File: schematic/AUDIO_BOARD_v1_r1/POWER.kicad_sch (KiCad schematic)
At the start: 10 parts, among them U20 DAC8565, U21 MCP23S17, U22 AP2112K-3.3

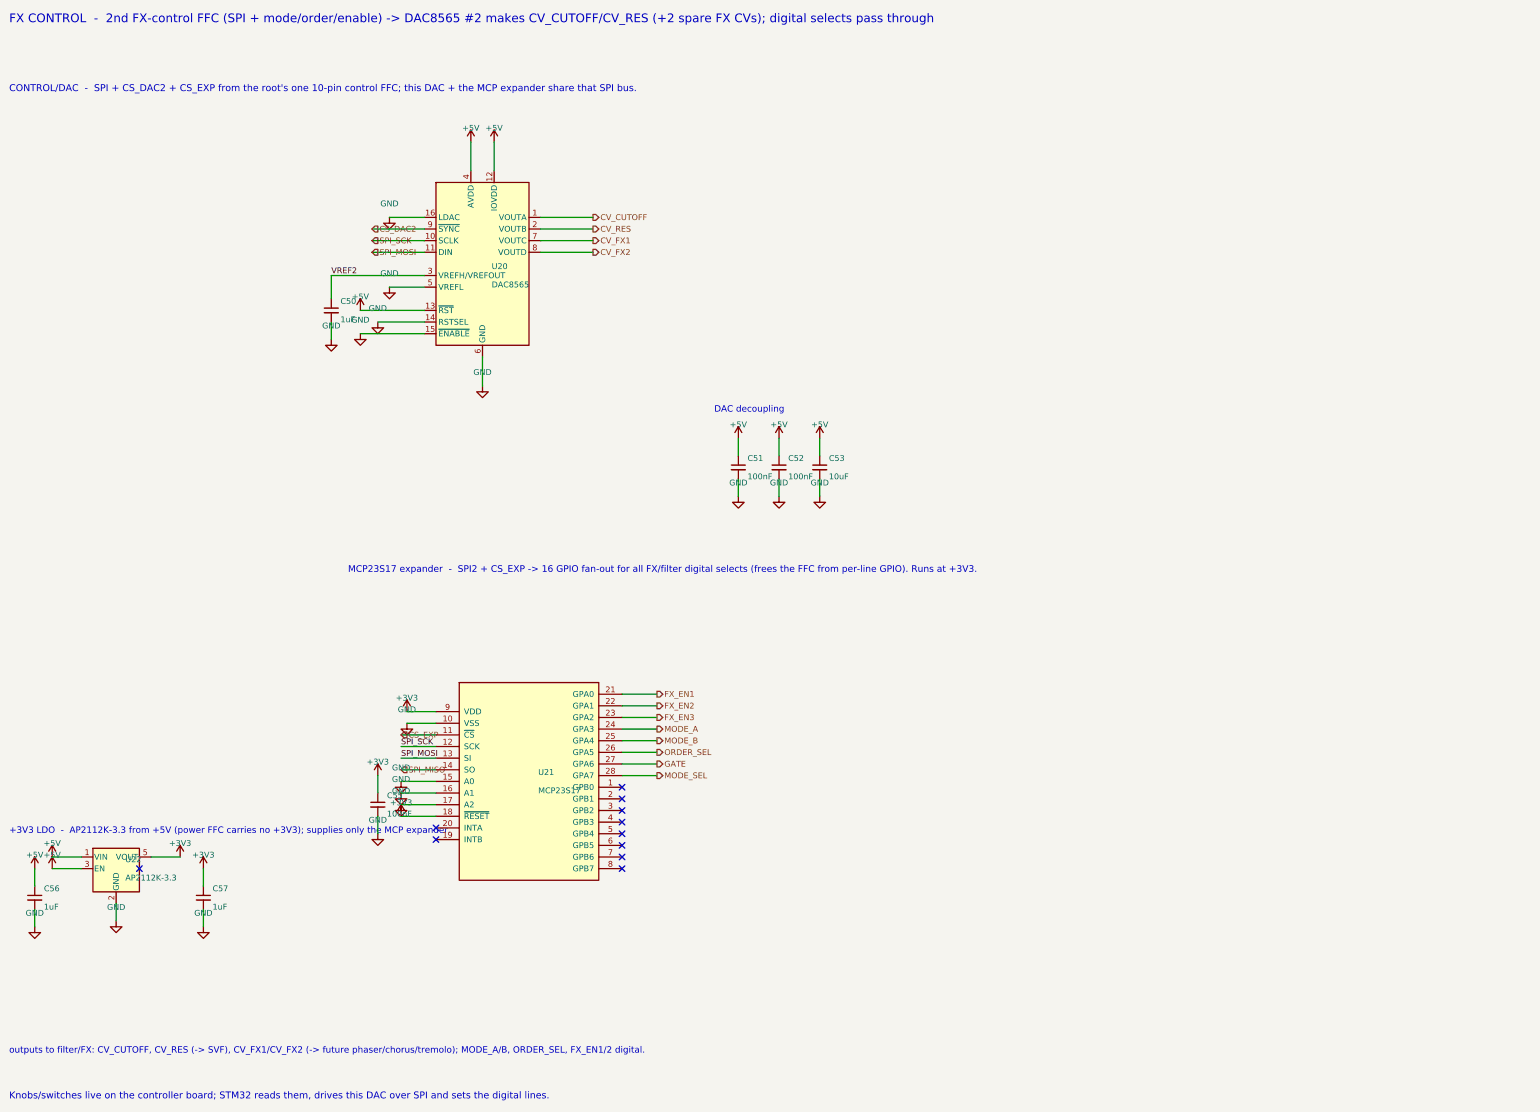
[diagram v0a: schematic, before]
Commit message: placing buffer for output. soft amp going, maybe AB rated. more routing
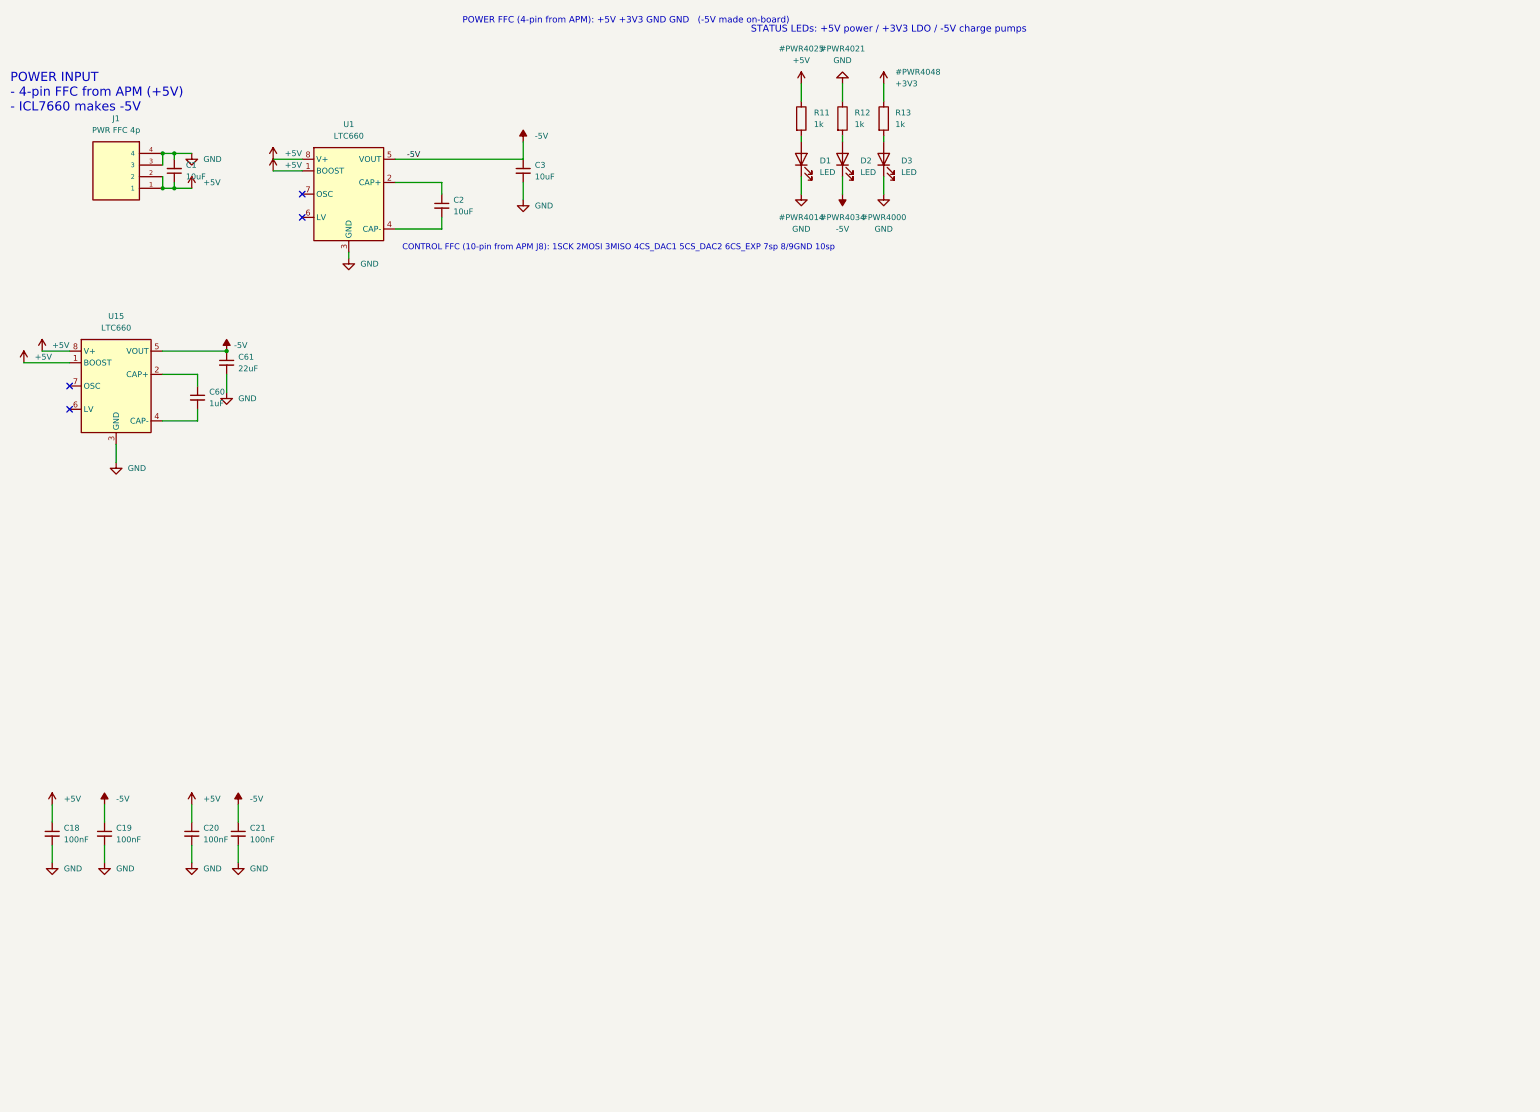
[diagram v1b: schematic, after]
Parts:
- removed C50, C56, C57: 1uF, Capacitor_SMD:C_0402_1005Metric, symbol Device:C_Small
- removed C51, C52, C55: 100nF, Capacitor_SMD:C_0402_1005Metric, symbol Device:C_Small
- removed C53: 10uF, Capacitor_SMD:C_0805_2012Metric, symbol Device:C_Small
- removed U20: DAC8565, Package_SO:TSSOP-16_4.4x5mm_P0.65mm, symbol Analog_DAC:DAC8565
- removed U21: MCP23S17, Package_SO:SOIC-28W_7.5x17.9mm_P1.27mm, symbol Custom:MCP23S17
- removed U22: AP2112K-3.3, Package_TO_SOT_SMD:SOT-23-5, symbol Regulator_Linear:AP2112K-3.3
- added C1, C2, C3: 10uF, Capacitor_SMD:C_0805_2012Metric, symbol Device:C_Small
- added C18, C19, C20, C21: 100nF, Capacitor_SMD:C_0402_1005Metric, symbol Device:C_Small
- added C60: 1uF, Capacitor_SMD:C_0805_2012Metric, symbol Device:C_Small
- added C61: 22uF, Capacitor_SMD:C_0805_2012Metric, symbol Device:C_Small
- added D1, D2, D3: LED, LED_SMD:LED_0603_1608Metric, symbol Device:LED
- added J1: PWR FFC 4p, my_footprints:AMPHENOL_F3311A7H121004E200, symbol F3311A7H121004E200:F3311A7H121004E200
- added R11, R12, R13: 1k, Resistor_SMD:R_0402_1005Metric, symbol Device:R
- added U1, U15: LTC660, Package_SO:SOIC-8_3.9x4.9mm_P1.27mm, symbol Regulator_SwitchedCapacitor:LTC660
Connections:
- net +3V3: now also R13.1
- net +5V: now also C1.1, C18.1, C20.1, J1.1, J1.2, R11.1, U1.1 (BOOST), U1.8 (V+), U15.1 (BOOST), U15.8 (V+)
- net GND: now also C1.2, C18.2, C19.2, C20.2, C21.2, C3.2, C61.2, D1.1 (K), D3.1 (K), J1.3, J1.4, R12.1, U1.3 (GND), U15.3 (GND)
- new net: C2.1, U1.2 (CAP+)
- new net: C2.2, U1.4 (CAP-)
- new net: D1.2 (A), R11.2
- new net: C60.1, U15.2 (CAP+)
- new net: C60.2, U15.4 (CAP-)
- new net: D2.2 (A), R12.2
- new net: D3.2 (A), R13.2
- new net -5V: C19.1, C21.1, C3.1, C61.1, D2.1 (K), U1.5 (VOUT), U15.5 (VOUT)
- no-connect marks 11 -> 4
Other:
- note added: "CONTROL FFC (10-pin from APM J8): 1SCK 2MOSI 3MISO 4CS_DAC1 5CS_DAC2 6CS_EXP 7sp 8/9GND 10sp"
- note added: "POWER FFC (4-pin from APM): +5V +3V3 GND GND (-5V made on-board)"
- note added: "POWER INPUT - 4-pin FFC from APM (+5V) - ICL7660 makes -5V"
- note added: "STATUS LEDs: +5V power / +3V3 LDO / -5V charge pumps"
- note removed: "+3V3 LDO - AP2112K-3.3 from +5V (power FFC carries no +3V3); supplies only the MCP expander."
- note removed: "CONTROL/DAC - SPI + CS_DAC2 + CS_EXP from the root's one 10-pin control FFC; this DAC + the MCP expander share that SPI bus."
- note removed: "DAC decoupling"
- note removed: "FX CONTROL - 2nd FX-control FFC (SPI + mode/order/enable) -> DAC8565 #2 makes CV_CUTOFF/CV_RES (+2 spare FX CVs); digital selects pass through"
- note removed: "Knobs/switches live on the controller board; STM32 reads them, drives this DAC over SPI and sets the digital lines."
- note removed: "MCP23S17 expander - SPI2 + CS_EXP -> 16 GPIO fan-out for all FX/filter digital selects (frees the FFC from per-line GPIO). Runs at +3V3."
- note removed: "outputs to filter/FX: CV_CUTOFF, CV_RES (-> SVF), CV_FX1/CV_FX2 (-> future phaser/chorus/tremolo); MODE_A/B, ORDER_SEL, FX_EN1/2 digital."

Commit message: more placement and routing
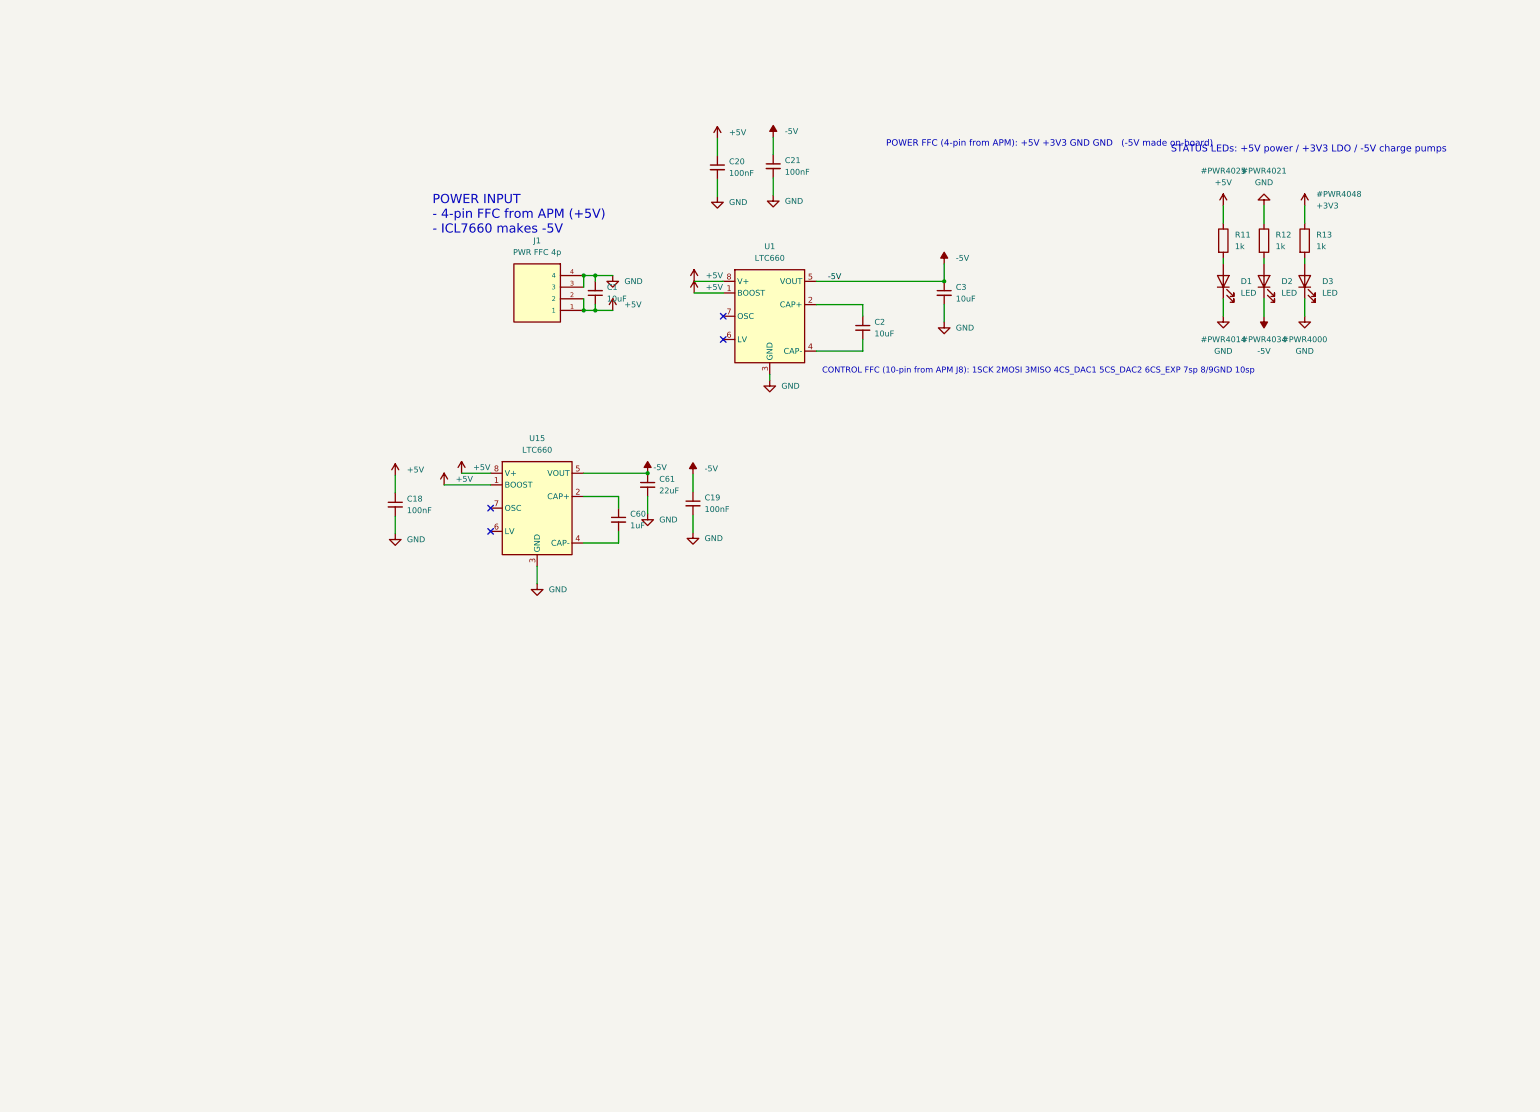
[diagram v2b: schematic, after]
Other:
- moved on the sheet: C1, C18, C19, C2, C20, C21, C3, C60, C61, D1, D2, D3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

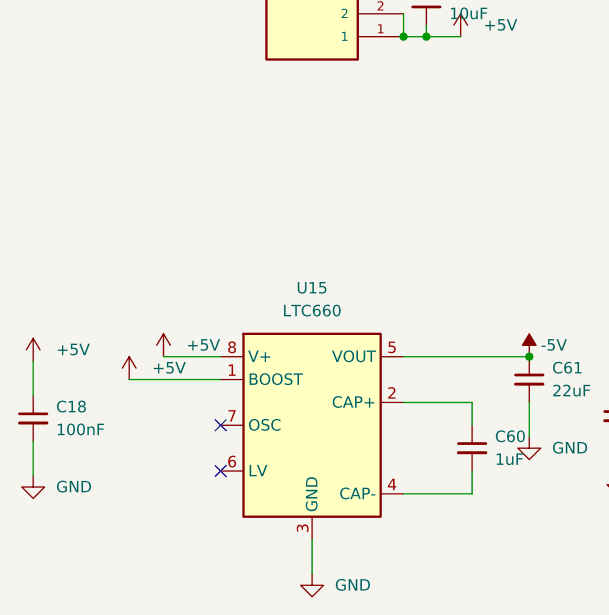
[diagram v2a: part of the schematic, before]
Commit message: placement. start with each sheet for the most part
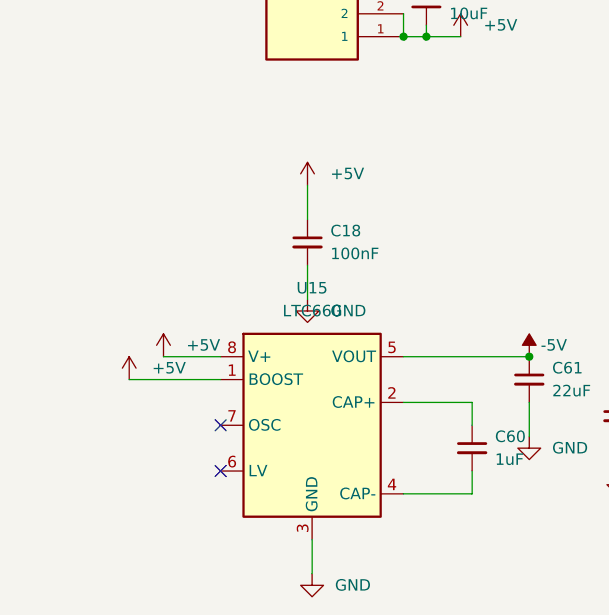
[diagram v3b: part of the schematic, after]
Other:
- moved on the sheet: C18
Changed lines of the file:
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@@
 	(wire
 		(pts
-			(xy 100.33 122.428) (xy 100.33 126.238)
+			(xy 130.81 102.87) (xy 130.81 106.68)
 		)
 		(stroke
@@
 	(wire
 		(pts
-			(xy 100.33 117.348) (xy 100.33 113.538)
+			(xy 130.81 97.79) (xy 130.81 93.98)
 		)
 		(stroke
@@
 	(symbol
 		(lib_id "power:+5V")
-		(at 100.33 113.538 0)
+		(at 130.81 93.98 0)
 		(unit 1)
 		(body_style 1)
@@
 		(fields_autoplaced yes)
 		(property "Reference" "#PWR4023"
-			(at 100.33 116.078 0)
+			(at 130.81 96.52 0)
 			(hide yes)
 			(show_name no)
@@
 		)
 		(property "Value" "+5V"
-			(at 102.87 112.268 0)
+			(at 133.35 92.71 0)
 			(show_name no)
 			(do_not_autoplace no)
@@
 		)
 		(property "Footprint" ""
-			(at 100.33 113.538 0)
+			(at 130.81 93.98 0)
 			(show_name no)
 			(do_not_autoplace no)
@@
 		)
 		(property "Datasheet" ""
-			(at 100.33 113.538 0)
+			(at 130.81 93.98 0)
 			(show_name no)
 			(do_not_autoplace no)
@@
 		)
 		(property "Description" ""
-			(at 100.33 113.538 0)
+			(at 130.81 93.98 0)
 			(show_name no)
 			(do_not_autoplace no)
@@
 	(symbol
 		(lib_id "power:GND")
-		(at 100.33 126.238 0)
+		(at 130.81 106.68 0)
 		(unit 1)
 		(body_style 1)
@@
 		(fields_autoplaced yes)
 		(property "Reference" "#PWR4040"
-			(at 100.33 128.778 0)
+			(at 130.81 109.22 0)
 			(hide yes)
 			(show_name no)
@@
 		)
 		(property "Value" "GND"
-			(at 102.87 127.508 0)
+			(at 133.35 107.95 0)
 			(show_name no)
 			(do_not_autoplace no)
@@
 		)
 		(property "Footprint" ""
-			(at 100.33 126.238 0)
+			(at 130.81 106.68 0)
 			(show_name no)
 			(do_not_autoplace no)
@@
 		)
 		(property "Datasheet" ""
-			(at 100.33 126.238 0)
+			(at 130.81 106.68 0)
 			(show_name no)
 			(do_not_autoplace no)
@@
 		)
 		(property "Description" ""
-			(at 100.33 126.238 0)
+			(at 130.81 106.68 0)
 			(show_name no)
 			(do_not_autoplace no)
@@
 	(symbol
 		(lib_id "Device:C_Small")
-		(at 100.33 119.888 0)
+		(at 130.81 100.33 0)
 		(unit 1)
 		(body_style 1)
@@
 		(fields_autoplaced yes)
 		(property "Reference" "C18"
-			(at 102.87 118.618 0)
+			(at 133.35 99.06 0)
 			(show_name no)
 			(do_not_autoplace no)
@@
 		)
 		(property "Value" "100nF"
-			(at 102.87 121.158 0)
+			(at 133.35 101.6 0)
 			(show_name no)
 			(do_not_autoplace no)
@@
 		)
 		(property "Footprint" "Capacitor_SMD:C_0402_1005Metric"
-			(at 100.33 119.888 0)
+			(at 130.81 100.33 0)
 			(hide yes)
 			(show_name no)
@@
 		)
 		(property "Datasheet" ""
-			(at 100.33 119.888 0)
+			(at 130.81 100.33 0)
 			(show_name no)
 			(do_not_autoplace no)
@@
 		)
 		(property "Description" ""
-			(at 100.33 119.888 0)
+			(at 130.81 100.33 0)
 			(show_name no)
 			(do_not_autoplace no)
